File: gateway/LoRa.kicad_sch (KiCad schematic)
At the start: 14 parts, among them IC901 MIC5317-3.3xM5, Q901 BSS123, X902 EC25

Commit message: Working on version 1.0
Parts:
- C901, C902: footprint (none) -> Capacitor_SMD:C_0805_2012Metric; manf (none) -> KYOCERA AVX; manf# (none) -> 08056C105MAT2A; mouser# (none) -> 581-08056C105MAT2A
- IC901: manf (none) -> Microchip Technology; manf# (none) -> MIC5317-3.3YM5-TR; mouser# (none) -> 998-MIC5317-3.3YM5-TR
- R901: footprint (none) -> Resistor_SMD:R_0805_2012Metric; manf (none) -> Bourns; manf# (none) -> CR0805-FX-1002GLF; mouser# (none) -> 652-CR0805-FX-1002GLF
- R902: renamed from R909; manf# CR0402-JW-680GLF -> CR0805-JW-680GLF; mouser# 652-CR0402-JW-680GLF -> 652-CR0805-JW-680GLF
- R903: renamed from R902; footprint (none) -> Resistor_SMD:R_0805_2012Metric; manf (none) -> Bourns; manf# (none) -> CR0805-JW-103GLF; mouser# (none) -> 652-CR0805-JW-103GLF
- R904: renamed from R903; footprint (none) -> Resistor_SMD:R_0805_2012Metric; manf (none) -> Bourns; manf# (none) -> CR0805-JW-103GLF; mouser# (none) -> 652-CR0805-JW-103GLF
- TP901: footprint (none) -> Testpoints_Kampi:TestPoint_Pad_1.0x1.0mm
- TP902: renamed from TP904; footprint (none) -> Testpoints_Kampi:TestPoint_Pad_1.0x1.0mm
- TP903: renamed from TP902; footprint (none) -> Testpoints_Kampi:TestPoint_Pad_1.0x1.0mm
- renumbered X902 to X903
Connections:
- net LoRa-Reset renamed LoRa-USB.Reset
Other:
- moved on the sheet: LED901, R902

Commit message: Working on PCB
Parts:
- added H901, H902: MountingHole, Wuerth:9774025151R, symbol Mechanical_Kampi:MountingHole
- added MP901: (no value), Bivar:SLP3-300-100-F, symbol Mechanical_Kampi:Light_Pipe
- X903: value EC25 -> LoRa
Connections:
- net LoRa-USB.D_N renamed LoRa.D_N
- net LoRa-USB.D_P renamed LoRa.D_P
- net LoRa-USB.Reset renamed LoRa.Reset

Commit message: Working on version 1.0.0
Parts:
- H901, H902: footprint Wuerth:9774025151R -> Wuerth:9774015151R; manf# 9774025151R -> 9774015151R; mouser# 710-9774025151R -> 710-9774015151R
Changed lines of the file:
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@@
 			)
 		)
-		(property "Footprint" "Wuerth:9774025151R"
+		(property "Footprint" "Wuerth:9774015151R"
 			(at 180.34 278.13 0)
 			(hide yes)
@@
 			)
 		)
-		(property "Datasheet" "https://www.we-online.com/components/products/datasheet/9774025151R.pdf"
+		(property "Datasheet" "https://www.we-online.com/components/products/datasheet/9774015151R.pdf"
 			(at 180.34 278.13 0)
 			(hide yes)
@@
 			)
 		)
-		(property "manf#" "9774025151R"
+		(property "manf#" "9774015151R"
 			(at 180.34 278.13 0)
 			(hide yes)
@@
 			)
 		)
-		(property "mouser#" "710-9774025151R"
+		(property "mouser#" "710-9774015151R"
 			(at 180.34 278.13 0)
 			(hide yes)
@@
 			)
 		)
-		(property "Footprint" "Wuerth:9774025151R"
+		(property "Footprint" "Wuerth:9774015151R"
 			(at 173.99 278.13 0)
 			(hide yes)
@@
 			)
 		)
-		(property "Datasheet" "https://www.we-online.com/components/products/datasheet/9774025151R.pdf"
+		(property "Datasheet" "https://www.we-online.com/components/products/datasheet/9774015151R.pdf"
 			(at 173.99 278.13 0)
 			(hide yes)
@@
 			)
 		)
-		(property "manf#" "9774025151R"
+		(property "manf#" "9774015151R"
 			(at 173.99 278.13 0)
 			(hide yes)
@@
 			)
 		)
-		(property "mouser#" "710-9774025151R"
+		(property "mouser#" "710-9774015151R"
 			(at 173.99 278.13 0)
 			(hide yes)
@@
 			(at 101.6 248.92 0)
 			(hide yes)
+			(show_name no)
+			(do_not_autoplace no)
+			(effects
+				(font
+					(size 1.27 1.27)
+				)
+			)
+		)
+		(property "Sim.Pins" "1=K 2=A"
+			(at 101.6 248.92 0)
+			(hide yes)

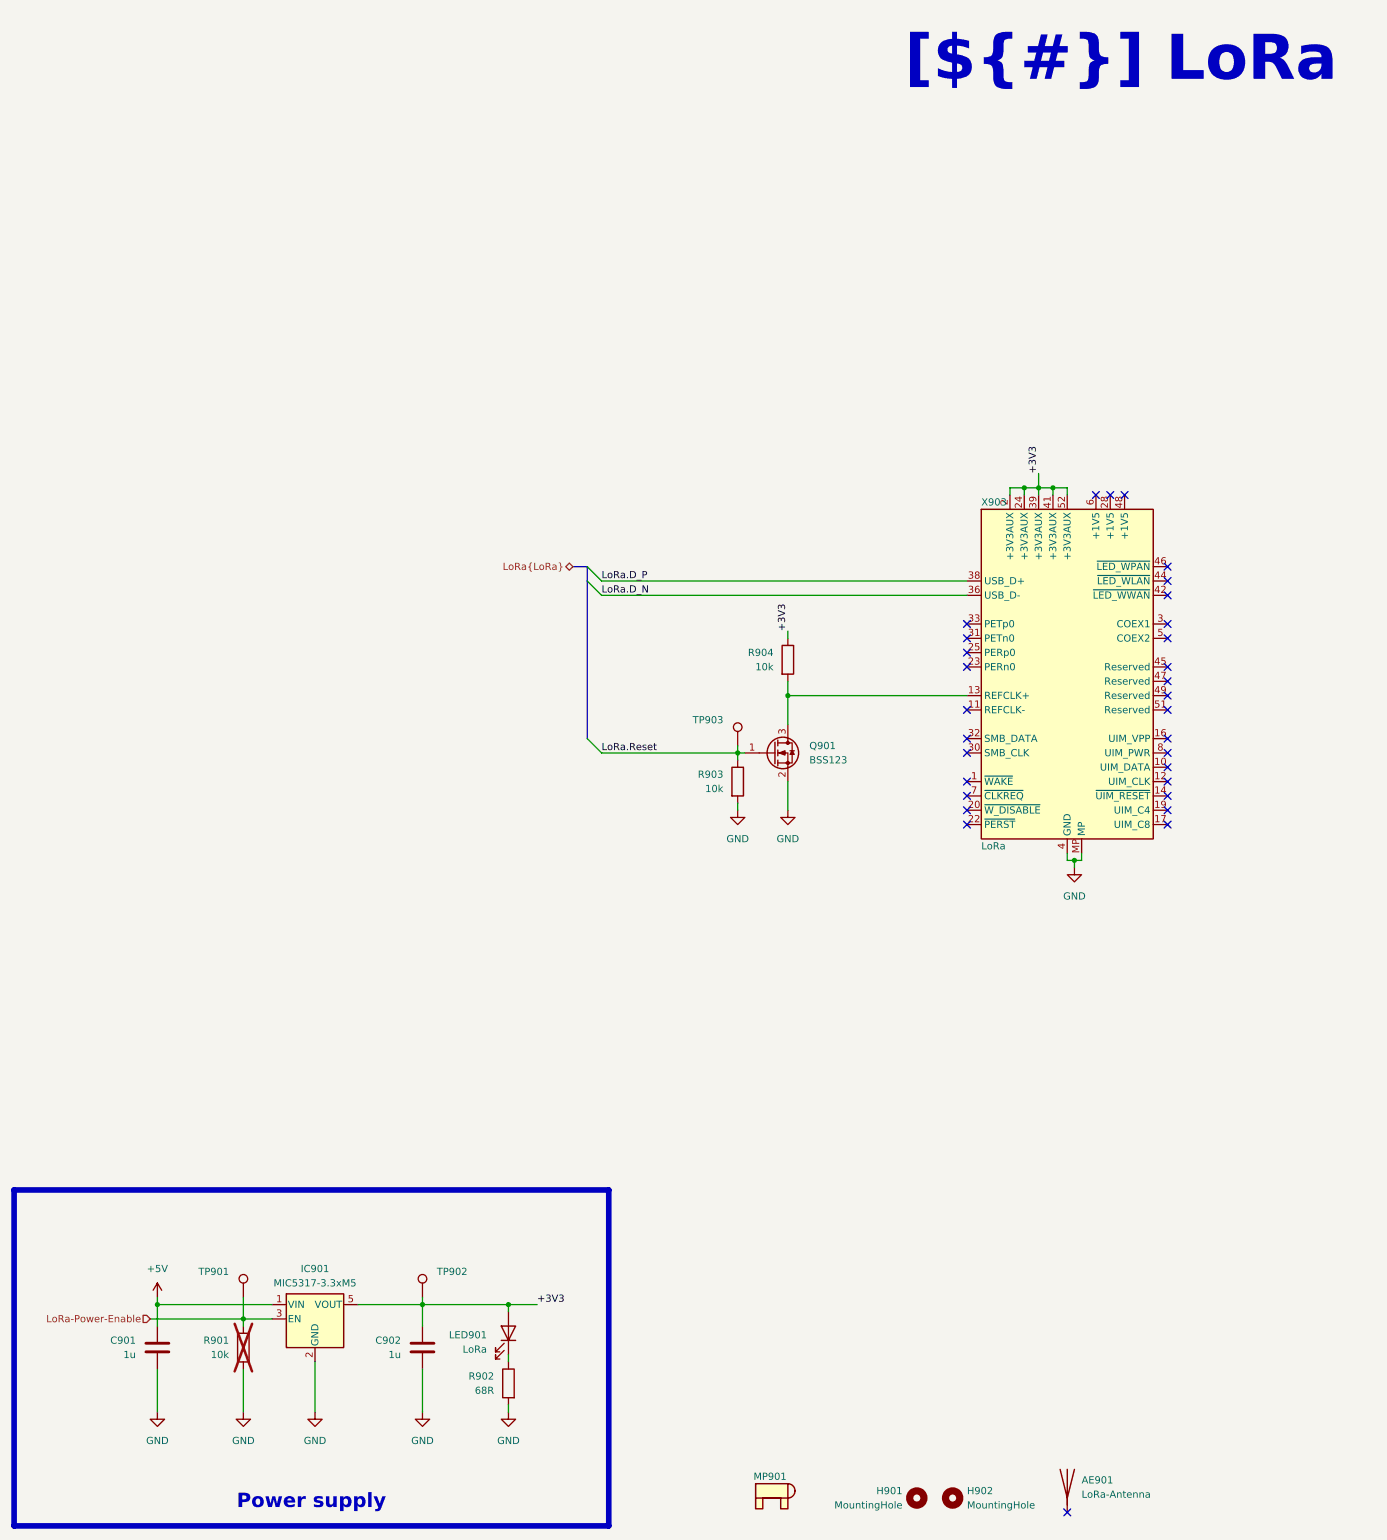
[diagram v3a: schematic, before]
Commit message: Replace level shifter, replace CC2530 with CC2652, fix wrong part numbers
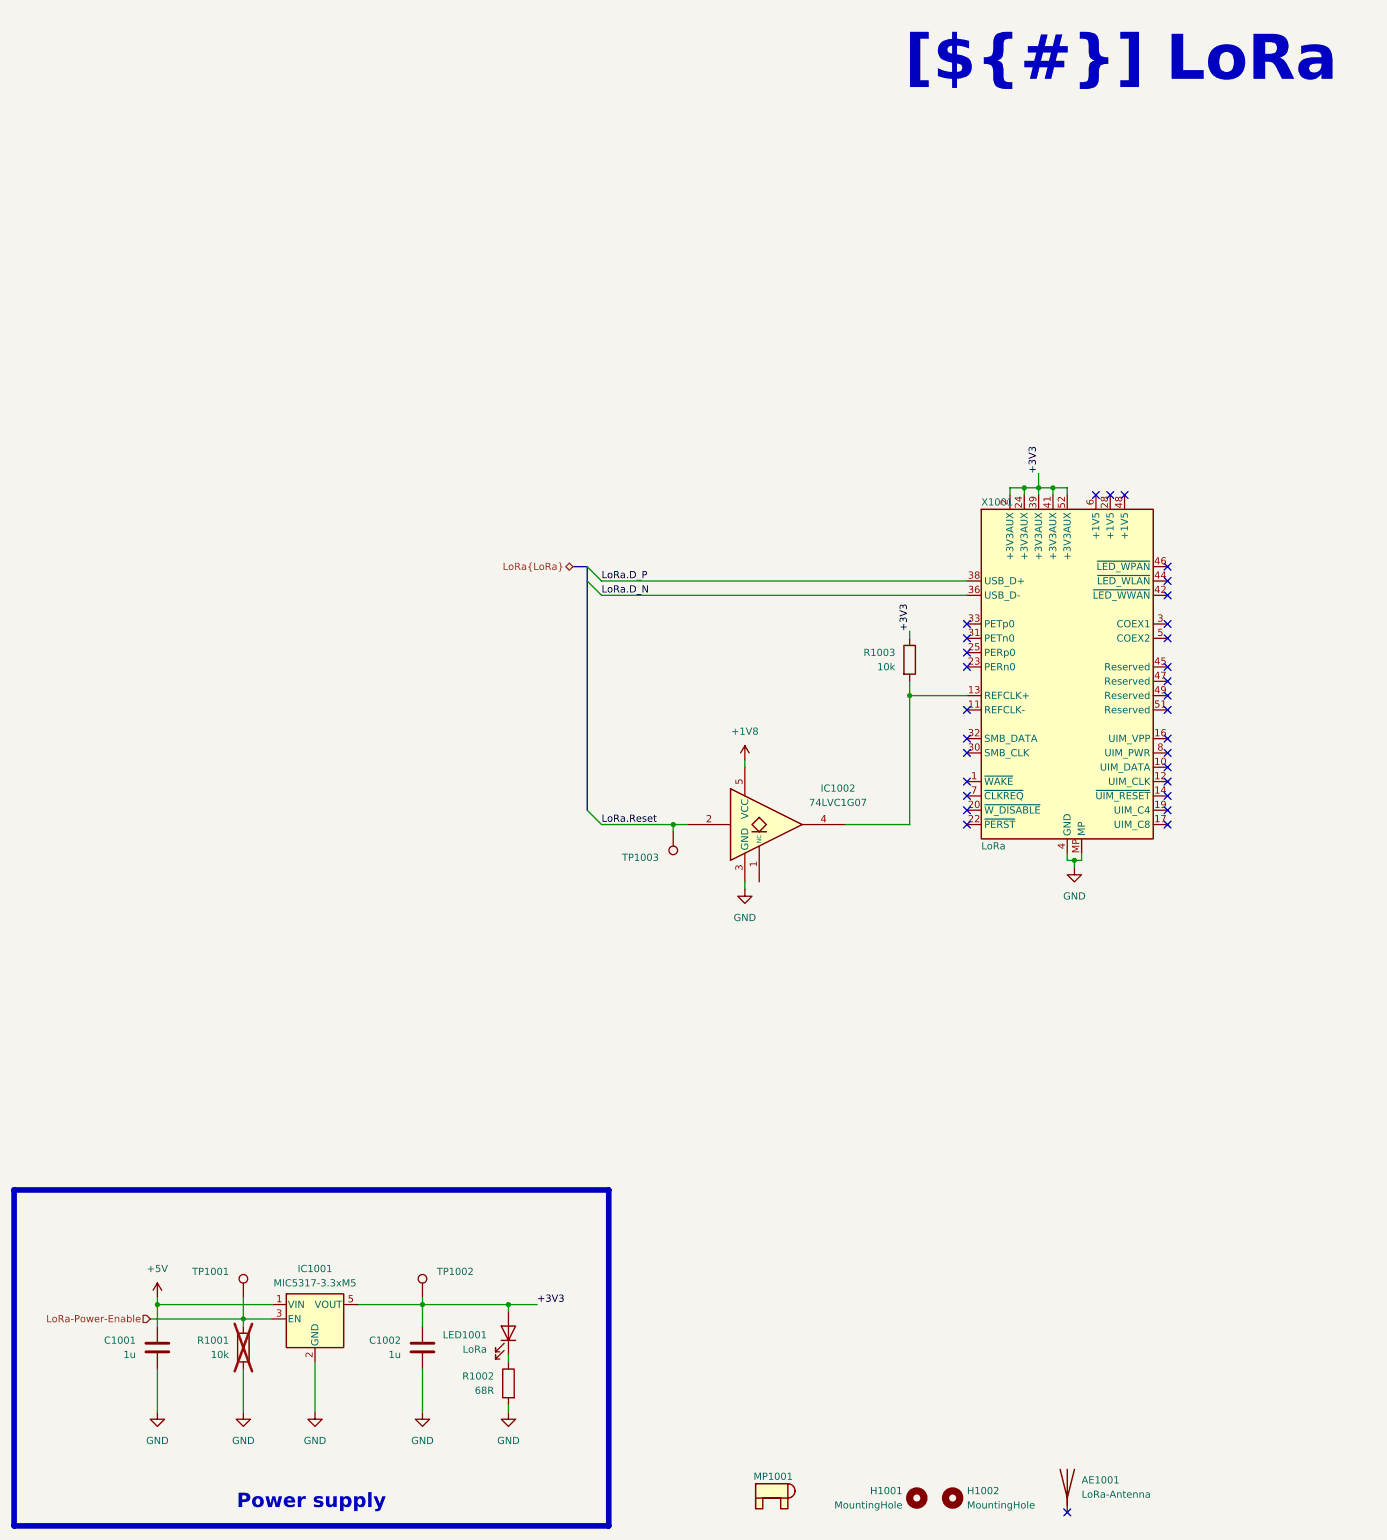
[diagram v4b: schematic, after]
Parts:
- removed Q901: BSS123, Package_TO_SOT_SMD:SOT-23, symbol Transistor_FET:BSS123
- removed R903: 10k, Resistor_SMD:R_0805_2012Metric, symbol Device:R
- added IC1002: 74LVC1G07, Package_TO_SOT_SMD:SOT-353_SC-70-5, symbol 74xGxx:74LVC1G07
- R1002: renamed from R902; footprint Resistor_SMD:R_0402_1005Metric -> Resistor_SMD:R_0805_2012Metric
- renumbered AE901 to AE1001, C901 to C1001, C902 to C1002, H901 to H1001, H902 to H1002, IC901 to IC1001, LED901 to LED1001, MP901 to MP1001, R901 to R1001, R904 to R1003, TP901 to TP1001, TP902 to TP1002, TP903 to TP1003, X903 to X1001
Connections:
- net GND: now also IC1002.3 (GND)
- net LoRa.Reset: now also IC1002.2
- net at R1003.2, X1001.13 (REFCLK+): now also IC1002.4
- new net +1V8: IC1002.5 (VCC)
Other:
- moved on the sheet: R1003, TP1003
